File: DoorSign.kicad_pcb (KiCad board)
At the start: 2 copper layers, 179.8 x 179.8 mm, 38 parts, among them J1 Wall, J2 Taster, J3 Taster-LED, U1 Pico, U2 PC817, U3 LM2575-5.0BT

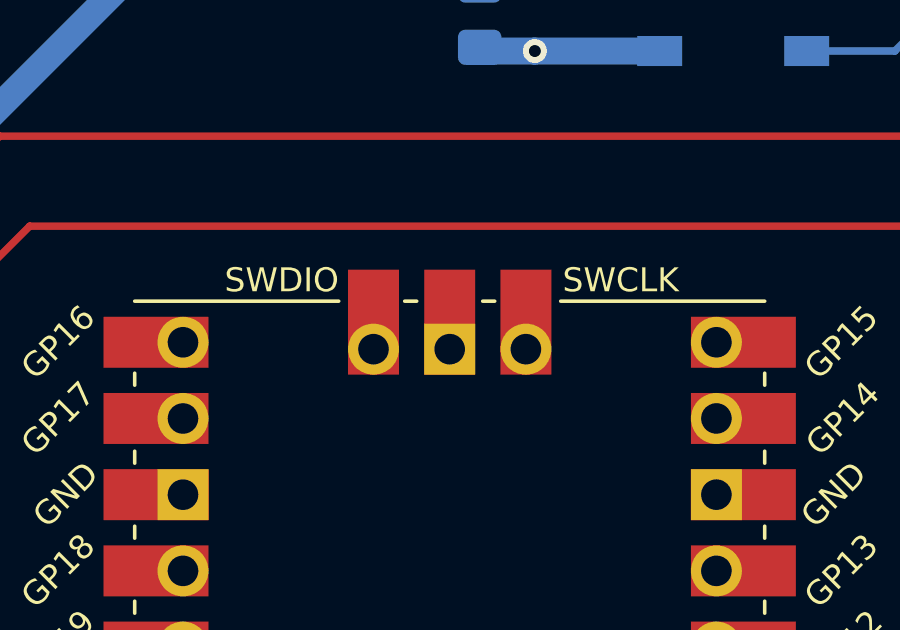
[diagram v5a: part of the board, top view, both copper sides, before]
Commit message: Modified footprints for compatibility with Pi Pico W
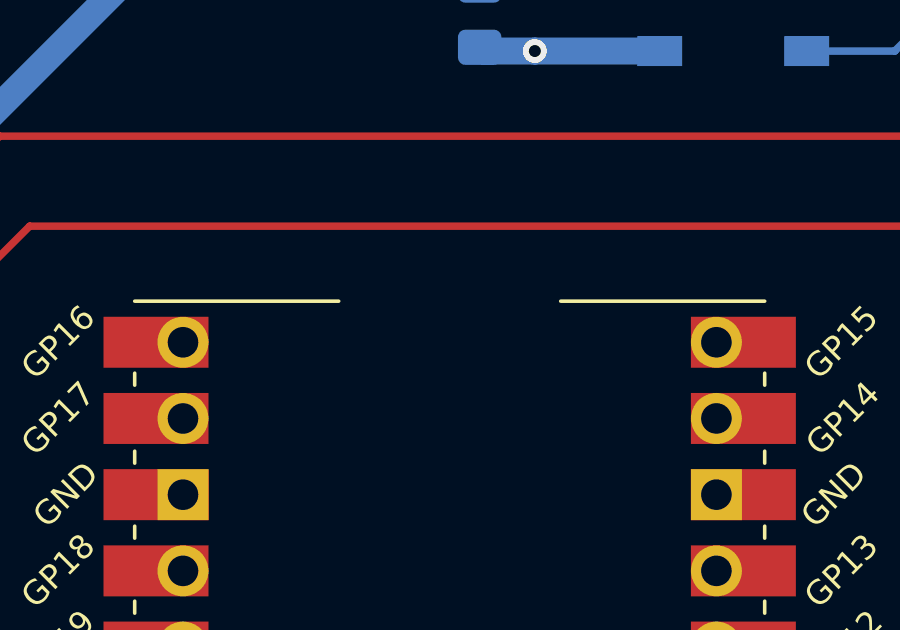
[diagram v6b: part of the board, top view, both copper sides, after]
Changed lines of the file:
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@@
   (net 49 "unconnected-(U1-Pad37)")
   (net 50 "unconnected-(U1-Pad40)")
-  (net 51 "unconnected-(U1-Pad41)")
-  (net 52 "unconnected-(U1-Pad43)")
   (footprint "Diode_THT:D_DO-41_SOD81_P10.16mm_Horizontal" (layer "F.Cu")
     (at 178.396975 114.112898 -135)
@@
       (effects (font (size 0.8 0.8) (thickness 0.15)))
     )
-    (fp_text user "SWCLK" (at -5.7 26.2) (layer "F.SilkS")
-      (effects (font (size 0.8 0.8) (thickness 0.15)))
-    )
-    (fp_text user "SWDIO" (at 5.6 26.2) (layer "F.SilkS")
-      (effects (font (size 0.8 0.8) (thickness 0.15)))
-    )
     (fp_text user "GP21" (at 13.054 8.9 45) (layer "F.SilkS")
       (effects (font (size 0.8 0.8) (thickness 0.15)))
@@
     (fp_line (start 10.5 -25.5) (end 10.5 -25.2) (layer "F.SilkS") (width 0.12))
     (fp_line (start -10.5 7.4) (end -10.5 7.8) (layer "F.SilkS") (width 0.12))
-    (fp_line (start 1.1 25.5) (end 1.5 25.5) (layer "F.SilkS") (width 0.12))
     (fp_line (start -10.5 -12.9) (end -10.5 -12.5) (layer "F.SilkS") (width 0.12))
     (fp_line (start -10.5 17.6) (end -10.5 18) (layer "F.SilkS") (width 0.12))
@@
     (fp_line (start 10.5 -10.4) (end 10.5 -10) (layer "F.SilkS") (width 0.12))
     (fp_line (start -10.5 15.1) (end -10.5 15.5) (layer "F.SilkS") (width 0.12))
-    (fp_line (start -1.5 25.5) (end -1.1 25.5) (layer "F.SilkS") (width 0.12))
     (fp_line (start -10.5 -23.1) (end -10.5 -22.7) (layer "F.SilkS") (width 0.12))
     (fp_line (start -10.5 -15.4) (end -10.5 -15) (layer "F.SilkS") (width 0.12))
@@
     (pad "40" thru_hole oval (at 8.89 -24.13 180) (size 1.7 1.7) (drill 1.02) (layers *.Cu *.Mask)
       (net 50 "unconnected-(U1-Pad40)") (pinfunction "VBUS") (pintype "power_in"))
-    (pad "41" thru_hole oval (at -2.54 23.9 180) (size 1.7 1.7) (drill 1.02) (layers *.Cu *.Mask)
-      (net 51 "unconnected-(U1-Pad41)") (pinfunction "SWCLK") (pintype "input"))
-    (pad "41" smd rect (at -2.54 23.9 270) (size 3.5 1.7) (drill (offset -0.9 0)) (layers "F.Cu" "F.Mask")
-      (net 51 "unconnected-(U1-Pad41)") (pinfunction "SWCLK") (pintype "input"))
-    (pad "42" smd rect (at 0 23.9 270) (size 3.5 1.7) (drill (offset -0.9 0)) (layers "F.Cu" "F.Mask")
-      (net 2 "GND") (pinfunction "GND") (pintype "power_in"))
-    (pad "42" thru_hole rect (at 0 23.9 180) (size 1.7 1.7) (drill 1.02) (layers *.Cu *.Mask)
-      (net 2 "GND") (pinfunction "GND") (pintype "power_in"))
-    (pad "43" thru_hole oval (at 2.54 23.9 180) (size 1.7 1.7) (drill 1.02) (layers *.Cu *.Mask)
-      (net 52 "unconnected-(U1-Pad43)") (pinfunction "SWDIO") (pintype "bidirectional"))
-    (pad "43" smd rect (at 2.54 23.9 270) (size 3.5 1.7) (drill (offset -0.9 0)) (layers "F.Cu" "F.Mask")
-      (net 52 "unconnected-(U1-Pad43)") (pinfunction "SWDIO") (pintype "bidirectional"))
     (model "C:/Users/ncara/OneDrive/IoT/Tools/KiCad/RP-Pico Libraries/Pico.wrl"
       (offset (xyz 0 0 0))
@@
     )
   )
+  (zone (net 0) (net_name "") (layer "F.Cu") (hatch edge 0.508)
+    (connect_pads (clearance 0))
+    (min_thickness 0.254)
+    (keepout (tracks not_allowed) (vias not_allowed) (pads not_allowed) (copperpour not_allowed) (footprints allowed))
+    (fill (thermal_gap 0.508) (thermal_bridge_width 0.508))
+    (polygon
+      (pts
+        (xy 57.577522 80.413437)
+        (xy 49.577522 80.413437)
+        (xy 49.577523 76.64705)
+        (xy 57.577523 76.64705)
+      )
+    )
+  )
   (zone (net 0) (net_name "") (layers F&B.Cu) (hatch edge 0.508)
     (connect_pads (clearance 0))
@@
       )
     )
+  )
+  (zone (net 0) (net_name "") (layer "F.Cu") (hatch edge 0.508)
+    (connect_pads (clearance 0))
+    (min_thickness 0.254)
+    (keepout (tracks not_allowed) (vias not_allowed) (pads not_allowed) (copperpour not_allowed) (footprints allowed))
+    (fill (thermal_gap 0.508) (thermal_bridge_width 0.508))
+    (polygon
+      (pts
+        (xy 62.375214 68.000001)
+        (xy 49.647303 68)
+        (xy 49.647303 57)
+        (xy 62.375214 57.000001)
+      )
+    )

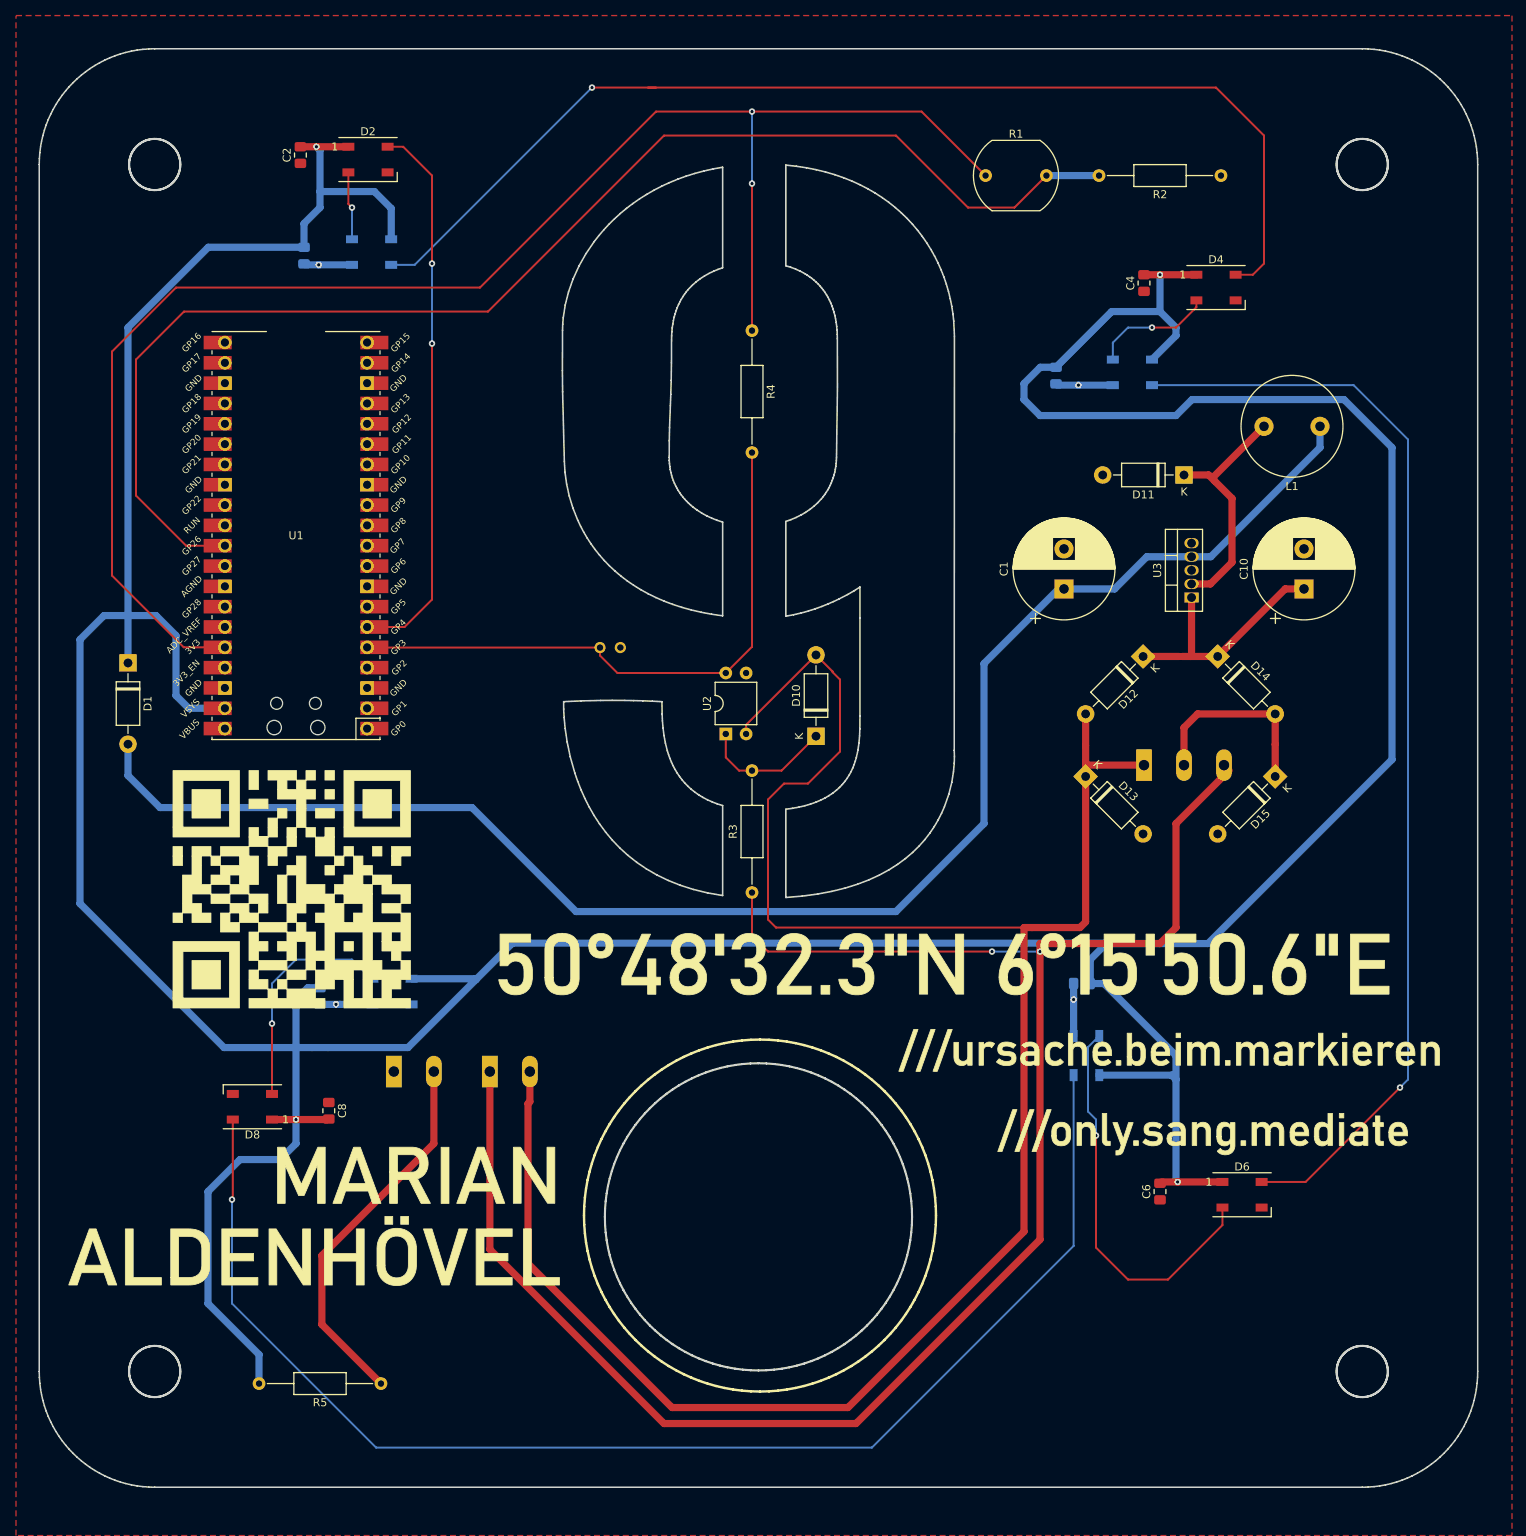
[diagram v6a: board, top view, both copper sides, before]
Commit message: Potential free contactor and pull-up/down added
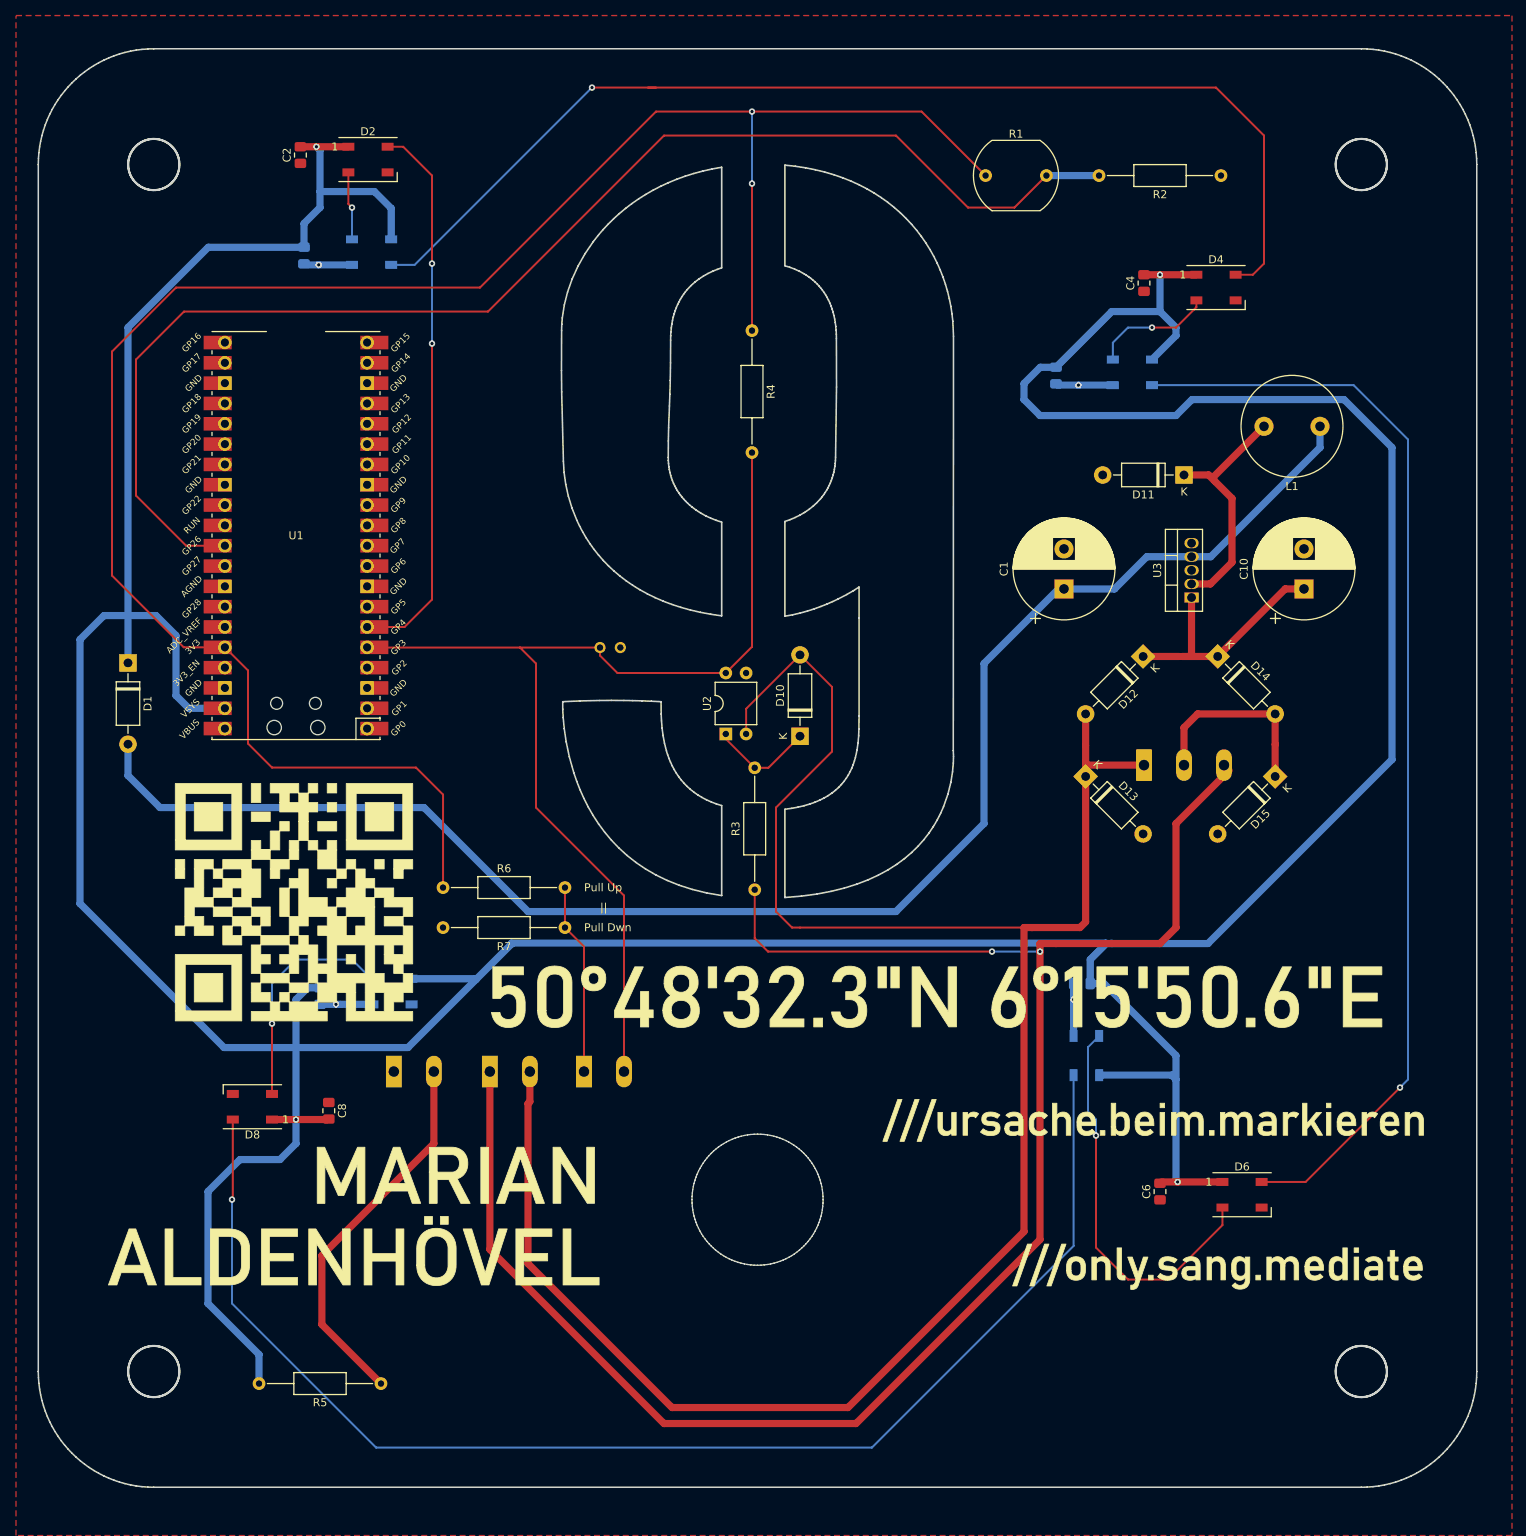
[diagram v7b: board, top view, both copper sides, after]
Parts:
- added J4: Taster B, TerminalBlock:TerminalBlock_Altech_AK300-2_P5.00mm, B.Cu at (92.0, 151.0)
- added R6: 10k, Resistor_THT:R_Axial_DIN0207_L6.3mm_D2.5mm_P15.24mm_Horizontal, F.Cu at (74.4, 128.0)
- added R7: 10k, Resistor_THT:R_Axial_DIN0207_L6.3mm_D2.5mm_P15.24mm_Horizontal, F.Cu at (89.6, 133.0)
- J2: value Taster -> Taster A
- moved D10 2.00 mm to (119.0, 109.1)
- moved R3 0.49 mm to (113.3, 128.3)
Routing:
- net Net-(J4-Pad2): track 75.7 -> 134.1 mm
- net +3.3V: track 198.1 -> 250.0 mm
- net Net-(J4-Pad1): track 0.00 -> 24.0 mm
- net /8VAC-L: track 268.8 -> 263.3 mm
- net Net-(D10-Pad1): track 16.7 -> 13.0 mm
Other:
- outline, holes or cut-outs redrawn
- board text added: "<-- Button GPIO"
- board text added: "<-- Button Ringer"
- board text added: "Pull Dwn"
- board text added: "Pull Up"
- board text added: "||"
- board text removed: "<-- Button"

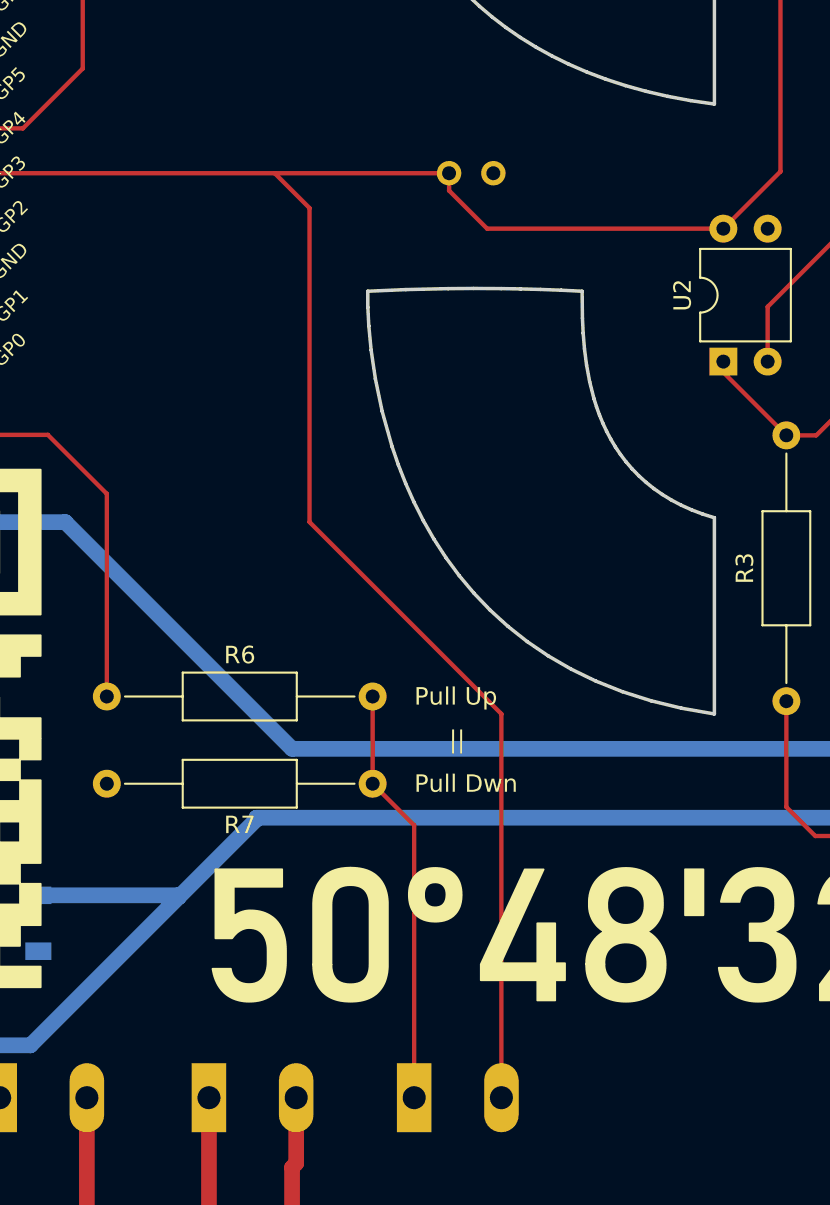
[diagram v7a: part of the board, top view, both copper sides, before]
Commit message: Jumpers for potential free contact
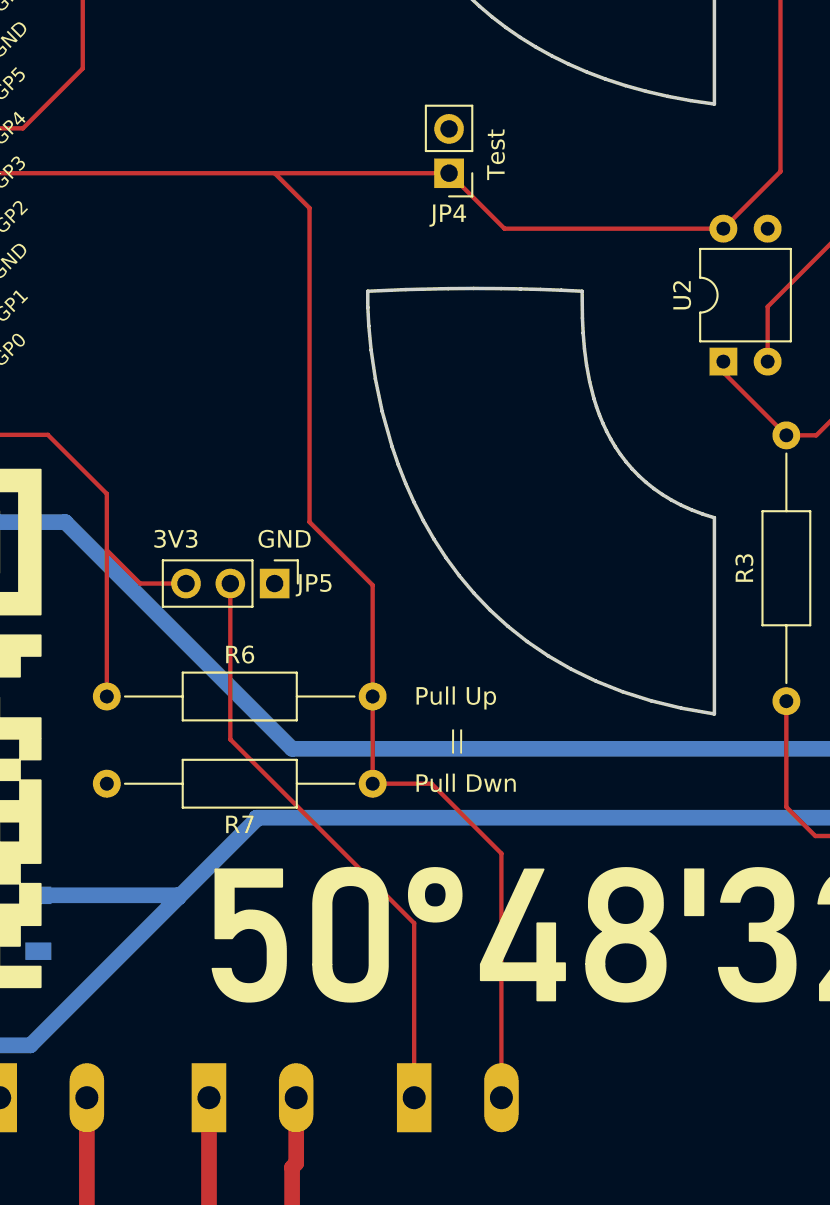
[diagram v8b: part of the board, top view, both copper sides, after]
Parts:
- added JP5: JP6, Connector_PinHeader_2.54mm:PinHeader_1x03_P2.54mm_Vertical, F.Cu at (84.0, 121.5)
- JP4: footprint TestPoint:TestPoint_2Pads_Pitch2.54mm_Drill0.8mm -> Connector_PinHeader_2.54mm:PinHeader_1x02_P2.54mm_Vertical; moved to F.Cu
- turned JP4 to 180 degrees
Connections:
- R6 pad 2: Net-(J4-Pad1) -> Net-(J4-Pad2)
- R7 pad 1: Net-(J4-Pad1) -> Net-(J4-Pad2)
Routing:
- net Net-(J4-Pad1): track 24.0 -> 33.8 mm
- net +3.3V: track 250.0 -> 255.3 mm
- net Net-(J4-Pad2): track 134.1 -> 135.4 mm
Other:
- board text added: "3V3"
- board text added: "GND"
